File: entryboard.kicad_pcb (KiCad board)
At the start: 2 copper layers, 74 x 57.5 mm, 25 parts, among them J1 Conn_01x01, J10 Conn_01x01, J11 Conn_01x01, J12 Conn_01x01, J13 Conn_01x03_Pin, J14 USB_C_Receptacle, J2 Conn_01x01, J3 Conn_01x01, J4 Conn_01x01, J5 Conn_01x01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

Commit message: feat: add headers for keys, and another ground point
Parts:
- added J15: Conn_01x03_Pin, Connector_PinHeader_1.00mm:PinHeader_1x03_P1.00mm_Vertical, F.Cu at (123.2, 41.0)
- added J16: Conn_01x01_Pin, Connector_PinHeader_1.00mm:PinHeader_1x01_P1.00mm_Vertical, F.Cu at (161.5, 43.0)
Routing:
- net DEVICE_POWER_BTN: track 11.3 -> 23.3 mm
- net DEVICE_VOL_UP: track 28.7 -> 37.3 mm
- net DEVICE_VOL_DOWN: track 44.9 -> 50.0 mm

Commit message: fix: Use 2.54mm pitch header pins
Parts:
- J13, J15: footprint Connector_PinHeader_1.00mm:PinHeader_1x03_P1.00mm_Vertical -> Connector_PinHeader_2.54mm:PinHeader_1x03_P2.54mm_Vertical
- J9: footprint Connector_PinHeader_1.00mm:PinHeader_1x02_P1.00mm_Vertical -> Connector_PinHeader_2.54mm:PinHeader_1x02_P2.54mm_Vertical
- moved J15 8.09 mm to (131.2, 41.5)
- moved J9 1.71 mm to (167.3, 68.5)
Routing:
- net DEVICE_VOL_DOWN: track 50.0 -> 58.7 mm
- net DEVICE_VOL_UP: track 37.3 -> 46.0 mm
- net DEVICE_POWER_BTN: track 23.3 -> 31.2 mm
- net UART_TX: track 34.0 -> 30.9 mm
- net DEVICE_USB_ID: track 2.50 -> 4.21 mm
- net UART_RX: track 36.5 -> 35.2 mm

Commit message: too much to say
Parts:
- removed J8: USB_A, Connector_USB:USB_A_Kycon_KUSBX-AS1N-B_Horizontal
- added R3: 3.3k, Resistor_SMD:R_1206_3216Metric_Pad1.30x1.75mm_HandSolder, F.Cu at (160.0, 58.0)
- added R4: 3.3k, Resistor_SMD:R_1206_3216Metric_Pad1.30x1.75mm_HandSolder, F.Cu at (141.8, 49.0)
- J1, J10, J11, J12, J2, J3, J4, J5: footprint TestPoint:TestPoint_Pad_1.0x1.0mm -> Connector_PinSocket_2.54mm:PinSocket_1x01_P2.54mm_Vertical
- J16: footprint Connector_PinHeader_1.00mm:PinHeader_1x01_P1.00mm_Vertical -> Connector_PinHeader_2.54mm:PinHeader_1x01_P2.54mm_Vertical
- moved J9 29.2 mm to (153.0, 43.0), turned to 90 degrees
- moved J1 3.00 mm to (171.5, 63.0)
- moved J5 2.75 mm to (171.5, 78.2)
- moved J2 1.75 mm to (171.5, 66.8)
- moved J3 1.25 mm to (171.5, 74.2), turned to 0 degrees
- moved J12 0.75 mm to (119.2, 44.0), turned to 0 degrees
- moved J10 0.65 mm to (111.8, 44.0), turned to 0 degrees
- moved J4 0.50 mm to (171.5, 70.5), turned to 0 degrees
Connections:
- J7 pad 1: UART_RX -> Net-(J7-Pin_1)
- J9 pad 1: DEVICE_USB_ID -> DEVICE_USB+
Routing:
- net DEVICE_USB-: track 35.7 -> 0.00 mm
- net +5V: track 78.4 -> 43.5 mm
- net GND: track 39.5 -> 16.3 mm, vias 19 -> 10
- net DEVICE_USB+: track 34.4 -> 50.1 mm
- net Net-(J7-Pin_1): track 0.00 -> 9.97 mm
- net UART_RX: track 35.2 -> 25.5 mm
- net DEVICE_USB_ID: track 4.21 -> 0.00 mm
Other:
- board text added: "EDL"

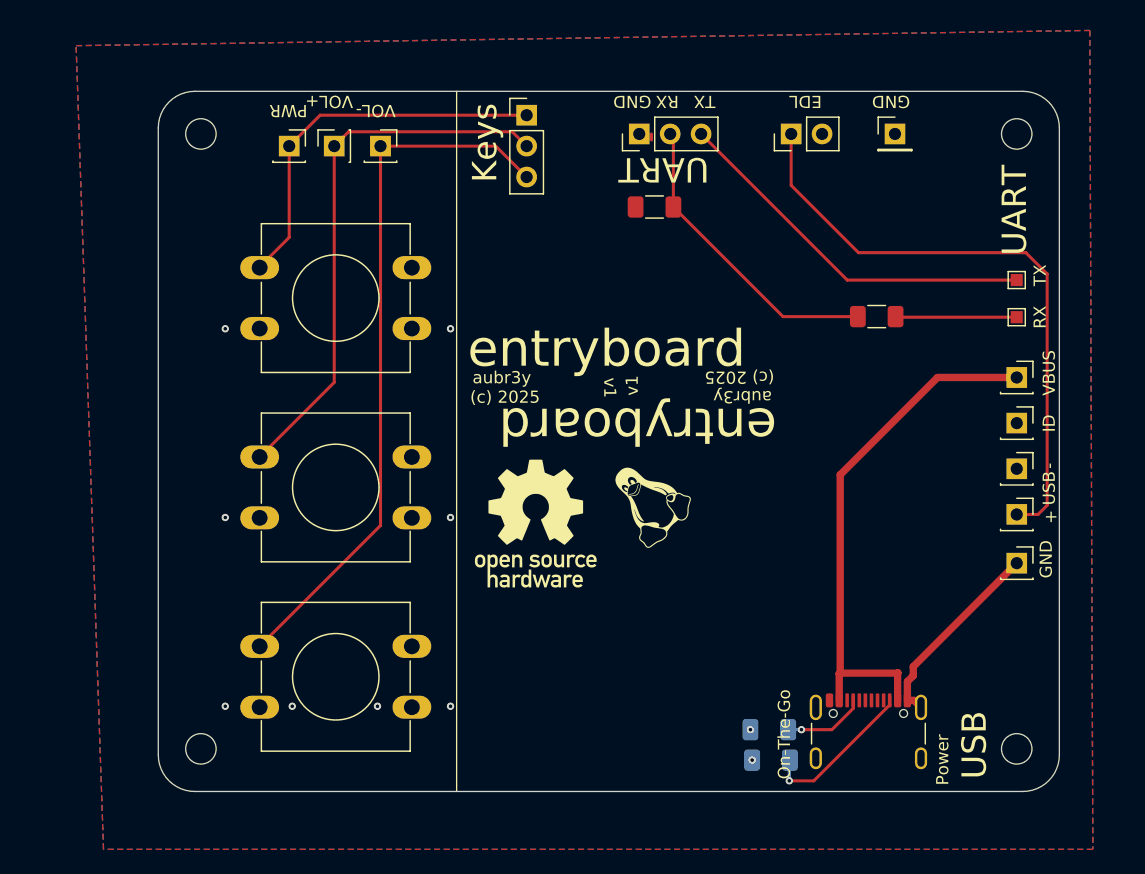
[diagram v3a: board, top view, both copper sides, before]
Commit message: refactor: drop usbs, smaller board
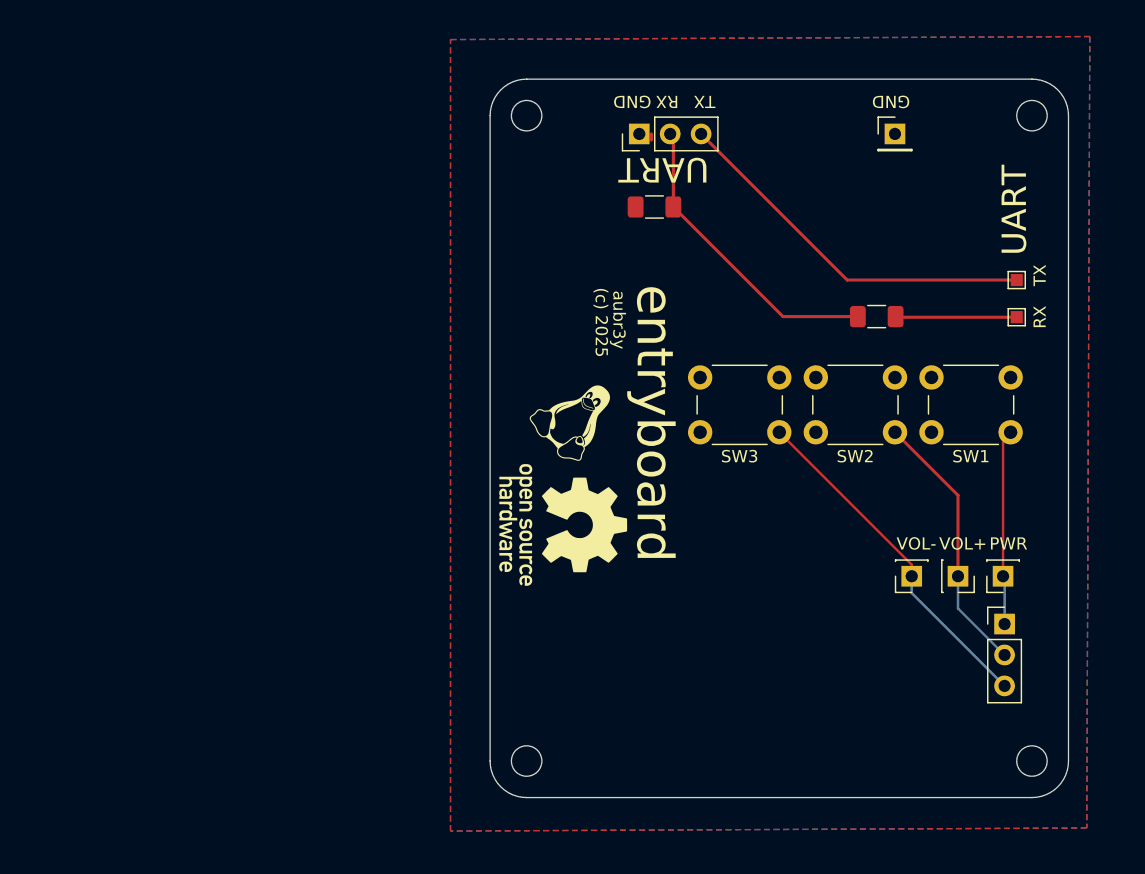
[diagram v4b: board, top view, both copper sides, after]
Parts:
- removed J1, J2, J3, J4, J5: Conn_01x01, Connector_PinSocket_2.54mm:PinSocket_1x01_P2.54mm_Vertical
- removed J14: USB_C_Receptacle, Connector_USB:USB_C_Receptacle_GCT_USB4105-xx-A_16P_TopMnt_Horizontal
- removed J9: Conn_01x02_Pin, Connector_PinHeader_2.54mm:PinHeader_1x02_P2.54mm_Vertical
- removed R1, R2: 5.1k, Resistor_SMD:R_1206_3216Metric_Pad1.30x1.75mm_HandSolder
- SW1, SW2, SW3: footprint Button_Switch_THT:SW_PUSH-12mm -> Button_Switch_THT:SW_PUSH_6mm
- moved J10 68.4 mm to (170.4, 79.3), turned to 180 degrees
- moved SW1 63.1 mm to (171.0, 67.5), turned to 180 degrees
- moved J11 62.2 mm to (166.7, 79.3), turned to -90 degrees
- moved J15 57.3 mm to (170.5, 83.2)
- moved J12 56.1 mm to (162.9, 79.3), turned to 180 degrees
- moved SW2 52.2 mm to (161.5, 67.5), turned to 180 degrees
- moved SW3 46.2 mm to (152.0, 67.5), turned to 180 degrees
- moved H1 26.8 mm to (131.2, 41.5)
- moved H4 26.8 mm to (131.2, 94.5)
- moved G*** 8.82 mm to (135.5, 66.1), turned to -45 degrees
- moved G*** 2.25 mm to (134.2, 75.1), turned to -90 degrees
- moved H2 1.95 mm to (172.8, 41.5)
- moved H3 1.60 mm to (172.8, 94.5)
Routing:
- net DEVICE_USB+: track 50.1 -> 0.00 mm
- net +5V: track 43.5 -> 0.00 mm
- net DEVICE_VOL_DOWN: track 58.2 -> 28.5 mm
- net DEVICE_VOL_UP: track 45.5 -> 22.0 mm
- net GND: track 16.3 -> 0.00 mm, vias 10 -> 0
- net DEVICE_POWER_BTN: track 31.5 -> 16.1 mm
- net Net-(J14-CC2): track 13.2 -> 0.00 mm, vias 1 -> 0
- net Net-(J14-CC1): track 6.99 -> 0.00 mm, vias 1 -> 0
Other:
- board size 74 x 57.5 mm -> 47.5 x 59 mm
- board text removed: "+"
- board text removed: "-"
- board text removed: "5.1k"
- board text removed: "EDL"
- board text removed: "ID"
- board text removed: "Keys"
- board text removed: "On-The-Go"
- board text removed: "Power"
- board text removed: "USB"
- board text removed: "VBUS"
- board text removed: "v1"

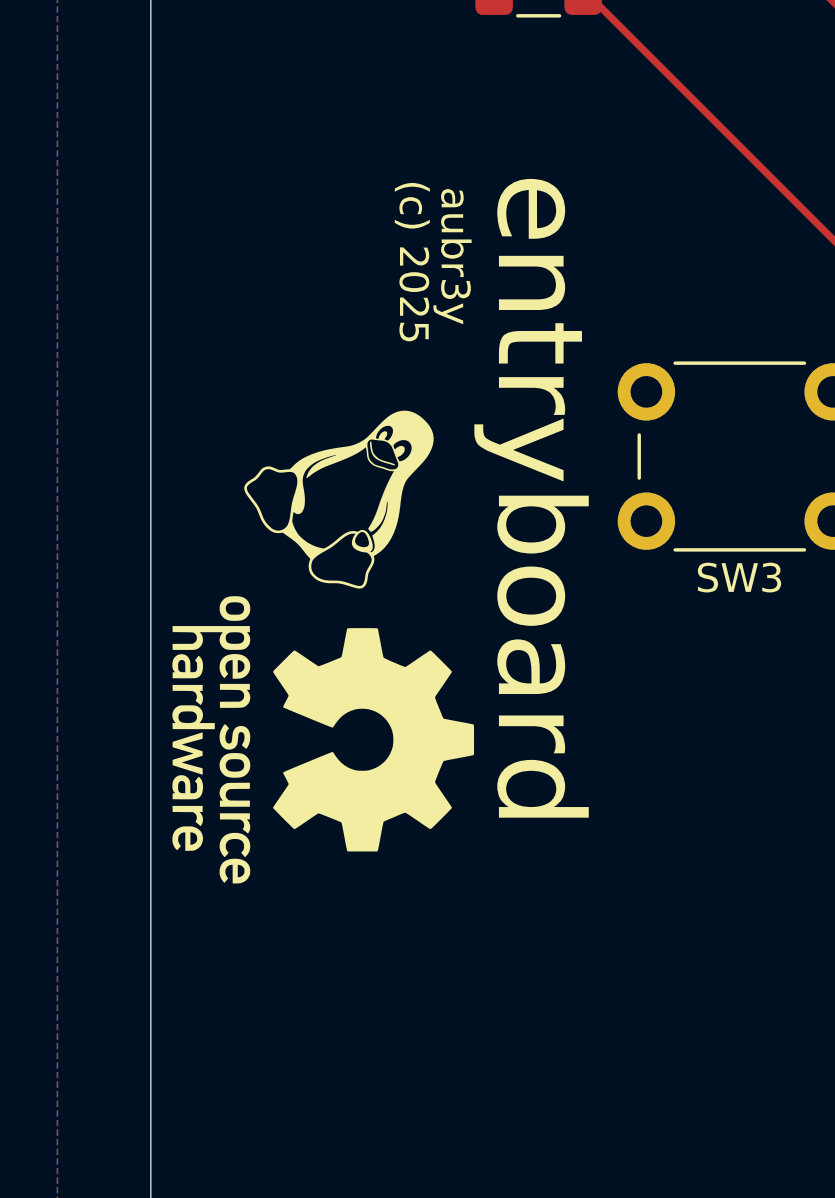
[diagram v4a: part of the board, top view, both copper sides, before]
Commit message: fix: make oshw farther from edge
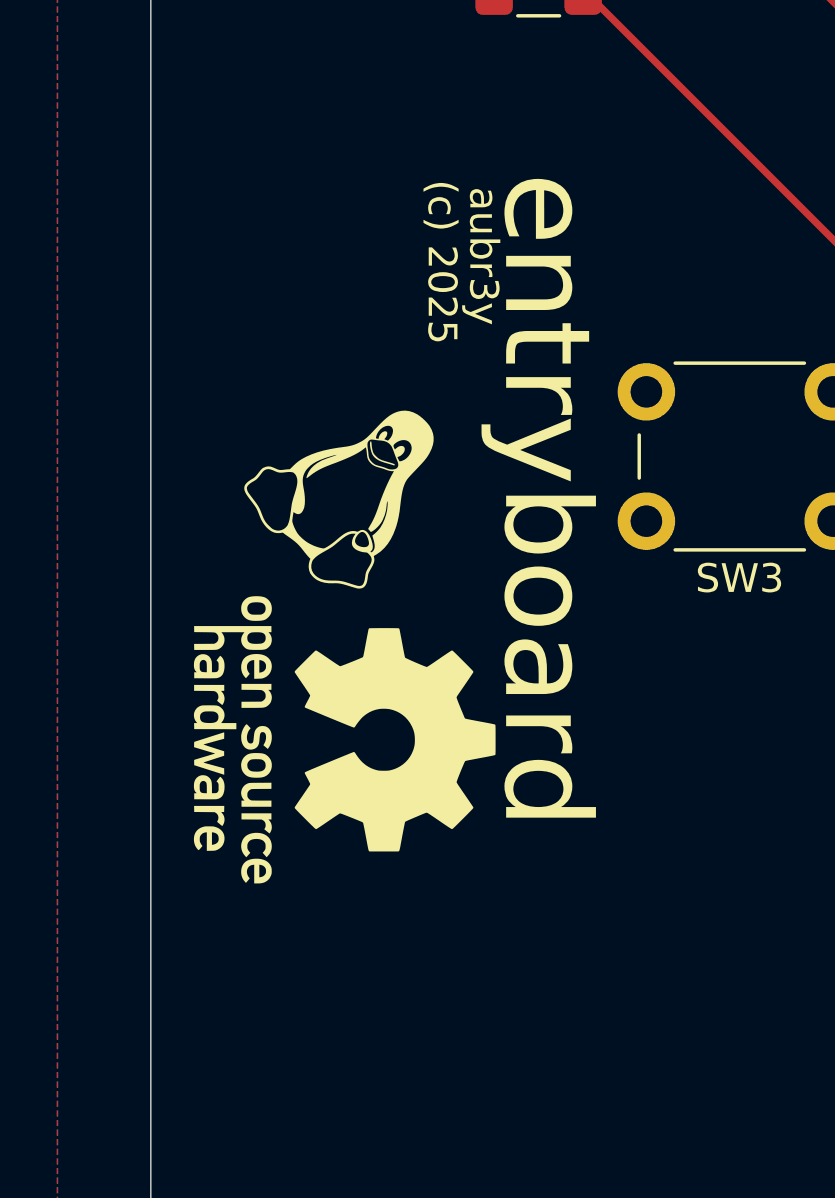
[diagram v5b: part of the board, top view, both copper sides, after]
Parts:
- moved G*** 0.75 mm to (135.0, 75.1)
